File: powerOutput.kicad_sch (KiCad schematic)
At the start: 25 parts, among them J1 Screw_Terminal_01x02, J10 Screw_Terminal_01x04, J11 Screw_Terminal_01x04, J12 Screw_Terminal_01x04, J9 Screw_Terminal_01x04, K1 SANYOU_SRD-S-124D, K2 SANYOU_SRD-S-124D, K3 SANYOU_SRD-S-124D, K4 SANYOU_SRD-S-124D, K5 SANYOU_SRD-S-124D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

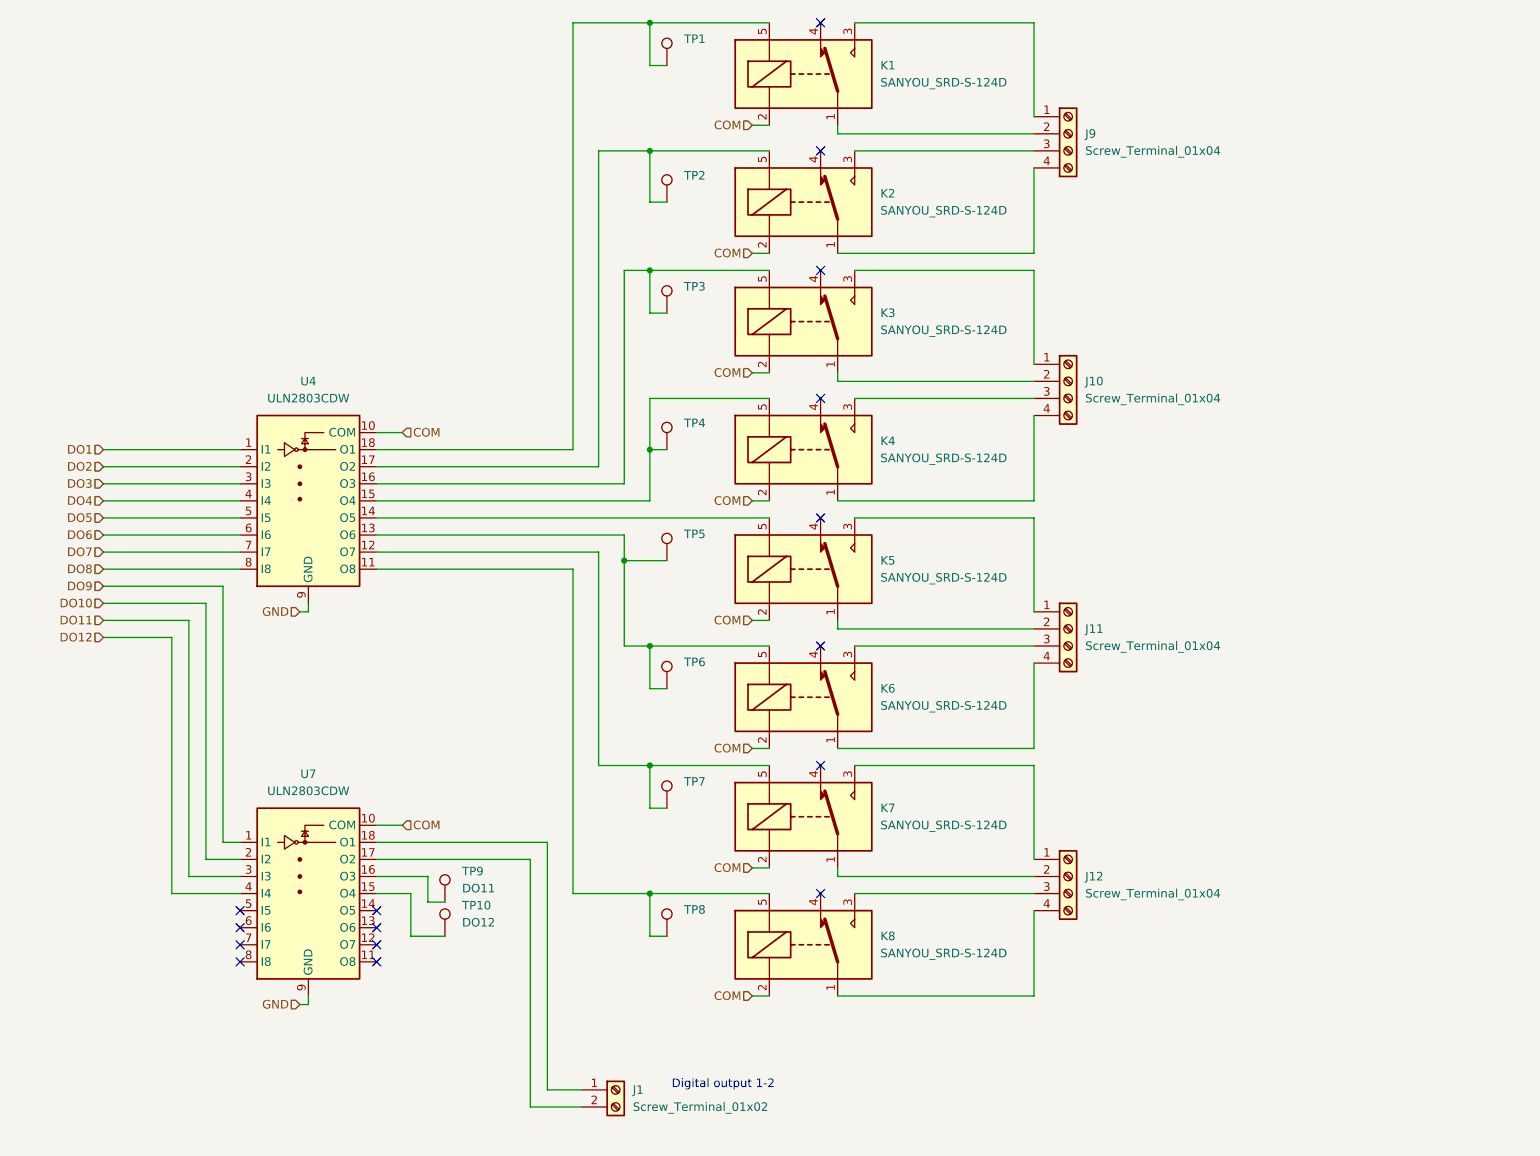
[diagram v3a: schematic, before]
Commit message: added fuse and c for 7805
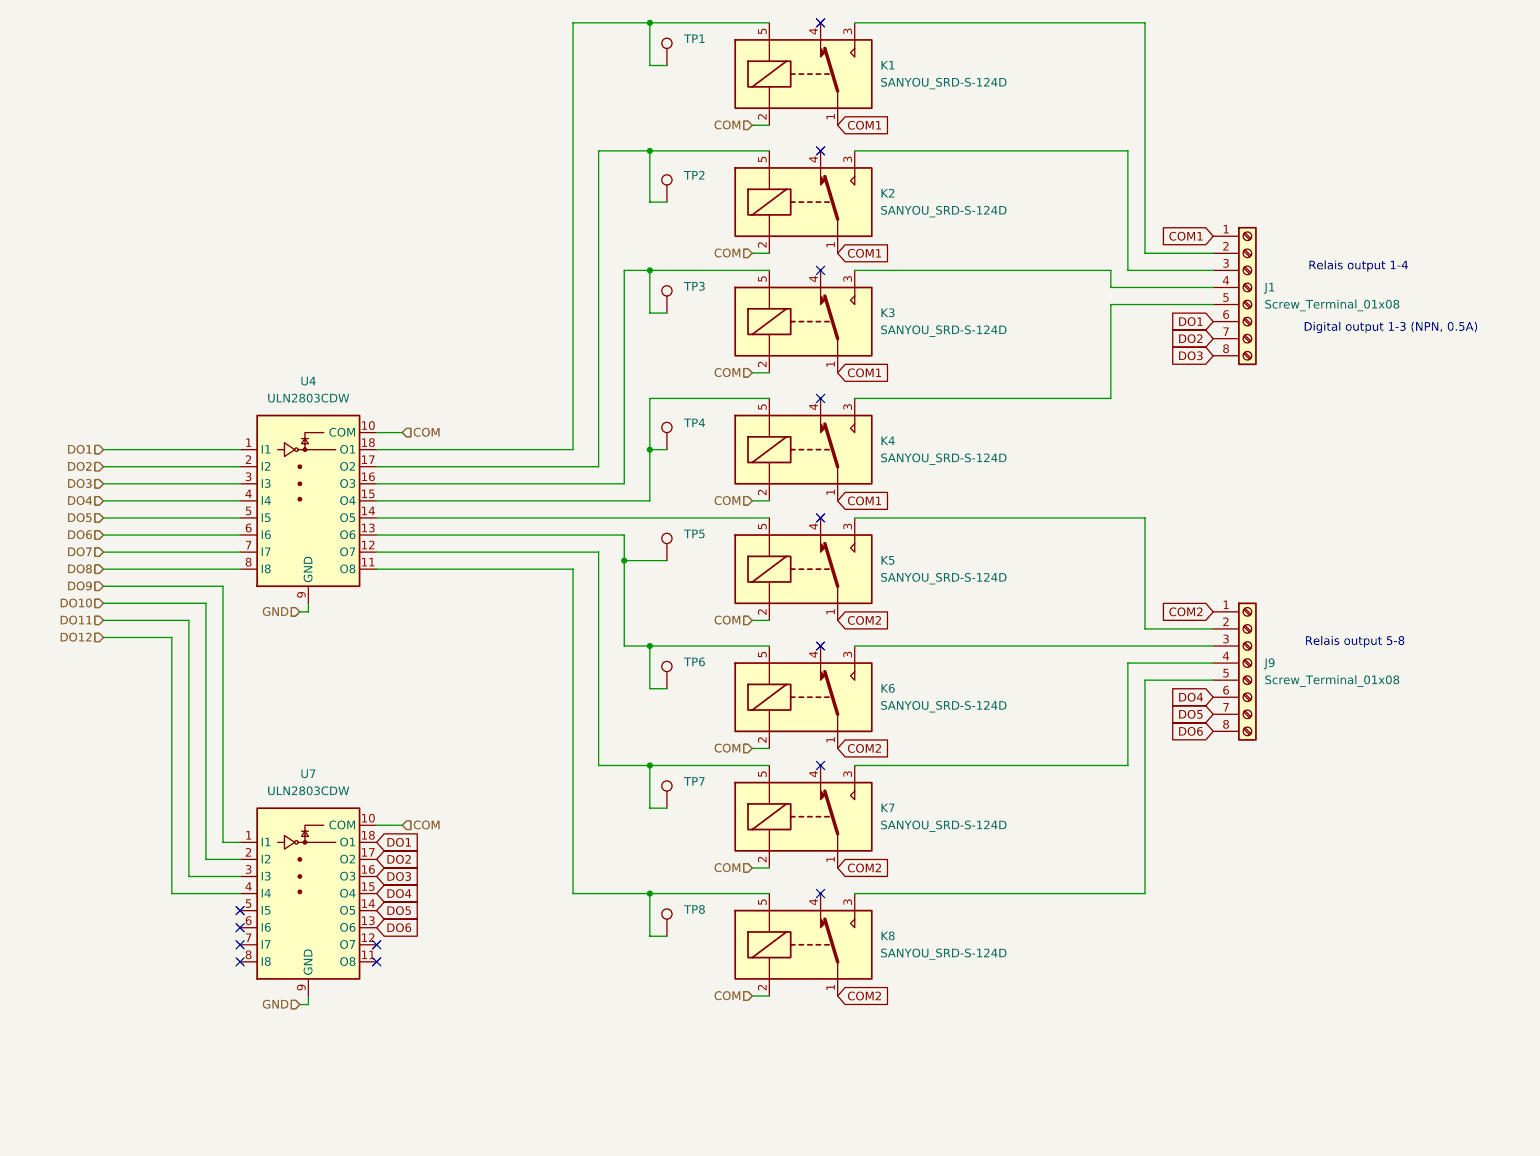
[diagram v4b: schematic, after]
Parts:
- removed J1: Screw_Terminal_01x02, Connector_Phoenix_MC:PhoenixContact_MC_1,5_2-G-3.5_1x02_P3.50mm_Horizontal, symbol Connector:Screw_Terminal_01x02
- removed J10, J11, J12, J9: Screw_Terminal_01x04, Connector_Phoenix_MC:PhoenixContact_MC_1,5_4-G-3.5_1x04_P3.50mm_Horizontal, symbol Connector:Screw_Terminal_01x04
- removed TP10: DO12, TestPoint:TestPoint_Plated_Hole_D2.0mm, symbol Connector:TestPoint
- removed TP9: DO11, TestPoint:TestPoint_Plated_Hole_D2.0mm, symbol Connector:TestPoint
- added J1, J9: Screw_Terminal_01x08, TerminalBlock_RND:TerminalBlock_RND_205-00293_1x08_P5.08mm_Horizontal, symbol Connector:Screw_Terminal_01x08
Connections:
- net DO1: now also U7.18 (O1), J1.6 (Pin_6)
- net DO2: now also U7.17 (O2), J1.7 (Pin_7)
- net DO3: now also U7.16 (O3), J1.8 (Pin_8)
- net DO4: now also U7.15 (O4), J9.6 (Pin_6)
- net DO5: now also U7.14 (O5), J9.7 (Pin_7)
- net DO6: now also U7.13 (O6), J9.8 (Pin_8)
- net at K5.3: now also J9.2 (Pin_2)
- net COM2: now reaches K5.1
- net COM2: now also K6.1, K7.1, K8.1, J9.1 (Pin_1)
- net at K6.3: now also J9.3 (Pin_3)
- net COM1: now reaches K1.1
- net COM1: now also K2.1, K3.1, K4.1, J1.1 (Pin_1)
- net at K1.3: now also J1.2 (Pin_2)
- net at K8.3: now also J9.5 (Pin_5)
- net at K2.3: now also J1.3 (Pin_3)
- net at K4.3: now also J1.5 (Pin_5)
- net at K7.3: now also J9.4 (Pin_4)
- net at K3.3: now also J1.4 (Pin_4)
- no-connect marks 16 -> 14
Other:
- note added: "Digital output 1-3 (NPN, 0.5A)"
- note added: "Relais output 1-4"
- note added: "Relais output 5-8"
- note removed: "Digital output 1-2"

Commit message: hat routing finished
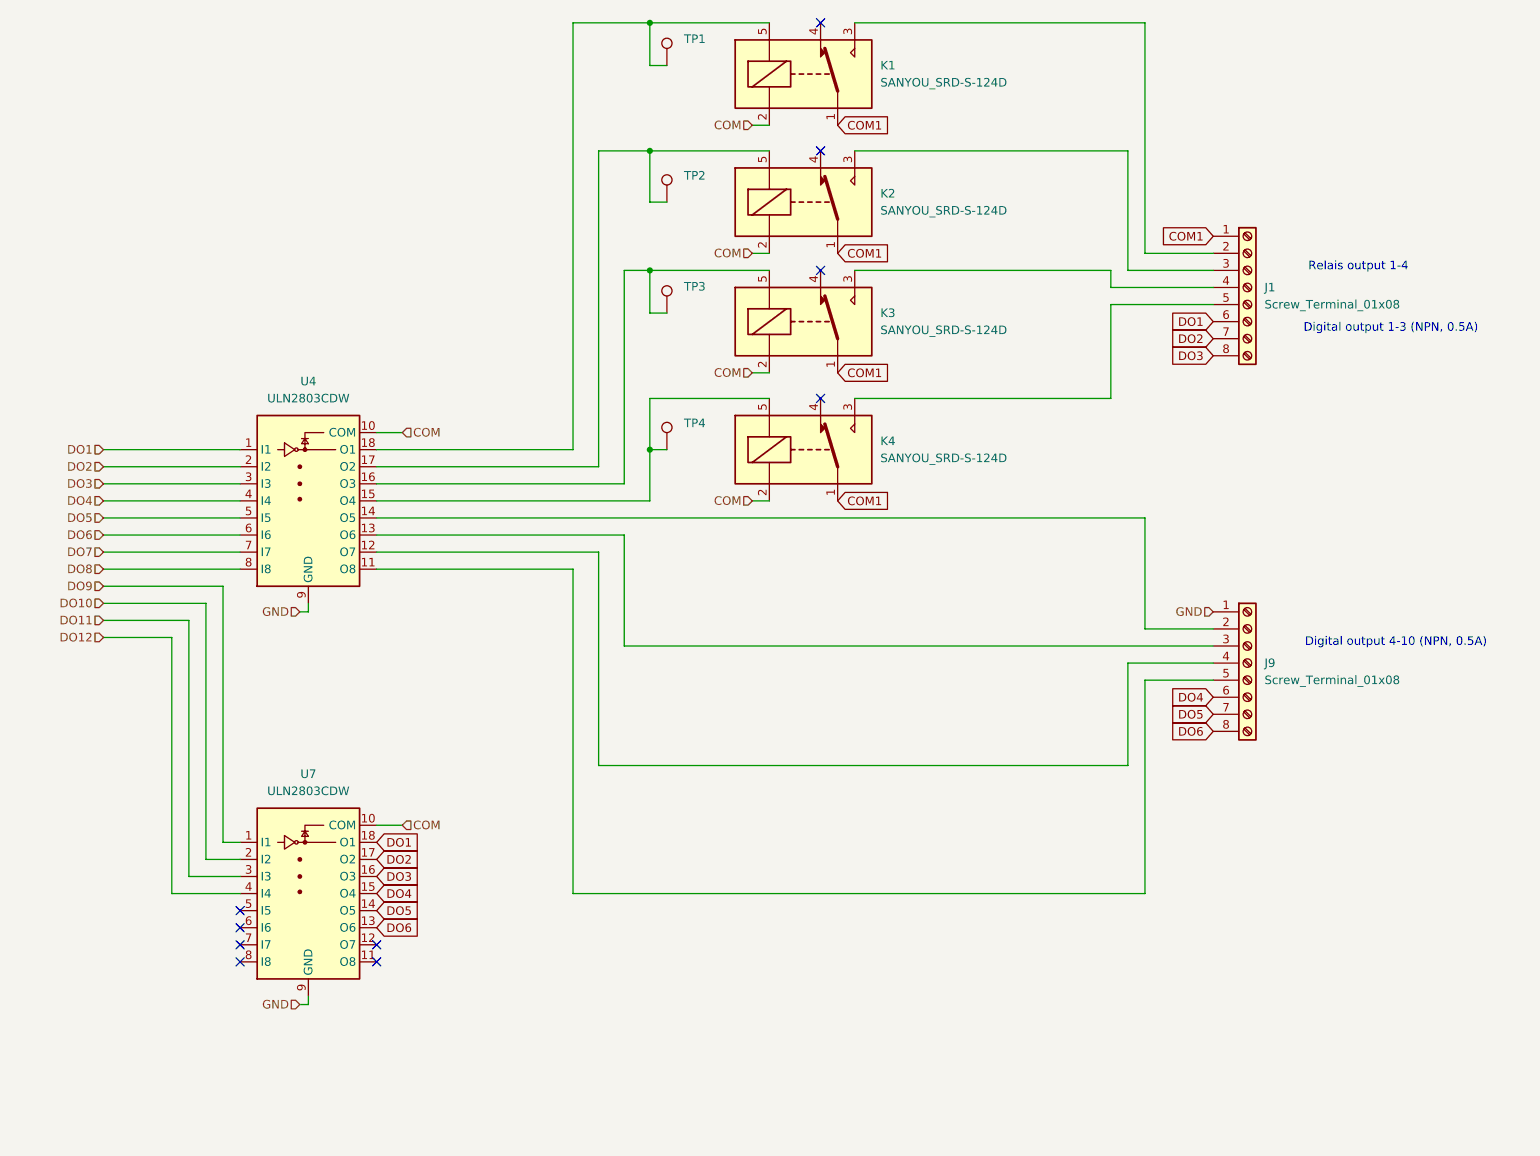
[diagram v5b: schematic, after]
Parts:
- removed K5, K6, K7, K8: SANYOU_SRD-S-124D, Relay_THT:Relay_SPDT_SANYOU_SRD_Series_Form_C, symbol Relay:SANYOU_SRD_Form_C
- removed TP5, TP6, TP7, TP8: ~, TestPoint:TestPoint_Pad_D1.5mm, symbol Connector:TestPoint
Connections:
- net COM2 is gone; now on net GND: J9.1 (Pin_1)
- net at U4.11 (O8): now also J9.5 (Pin_5)
- net at U4.12 (O7): now also J9.4 (Pin_4)
- net at J9.2 (Pin_2): now also U4.14 (O5)
- net at J9.3 (Pin_3): now also U4.13 (O6)
- no-connect marks 14 -> 10
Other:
- note added: "Digital output 4-10 (NPN, 0.5A)"
- note removed: "Relais output 5-8"

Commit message: started base layout
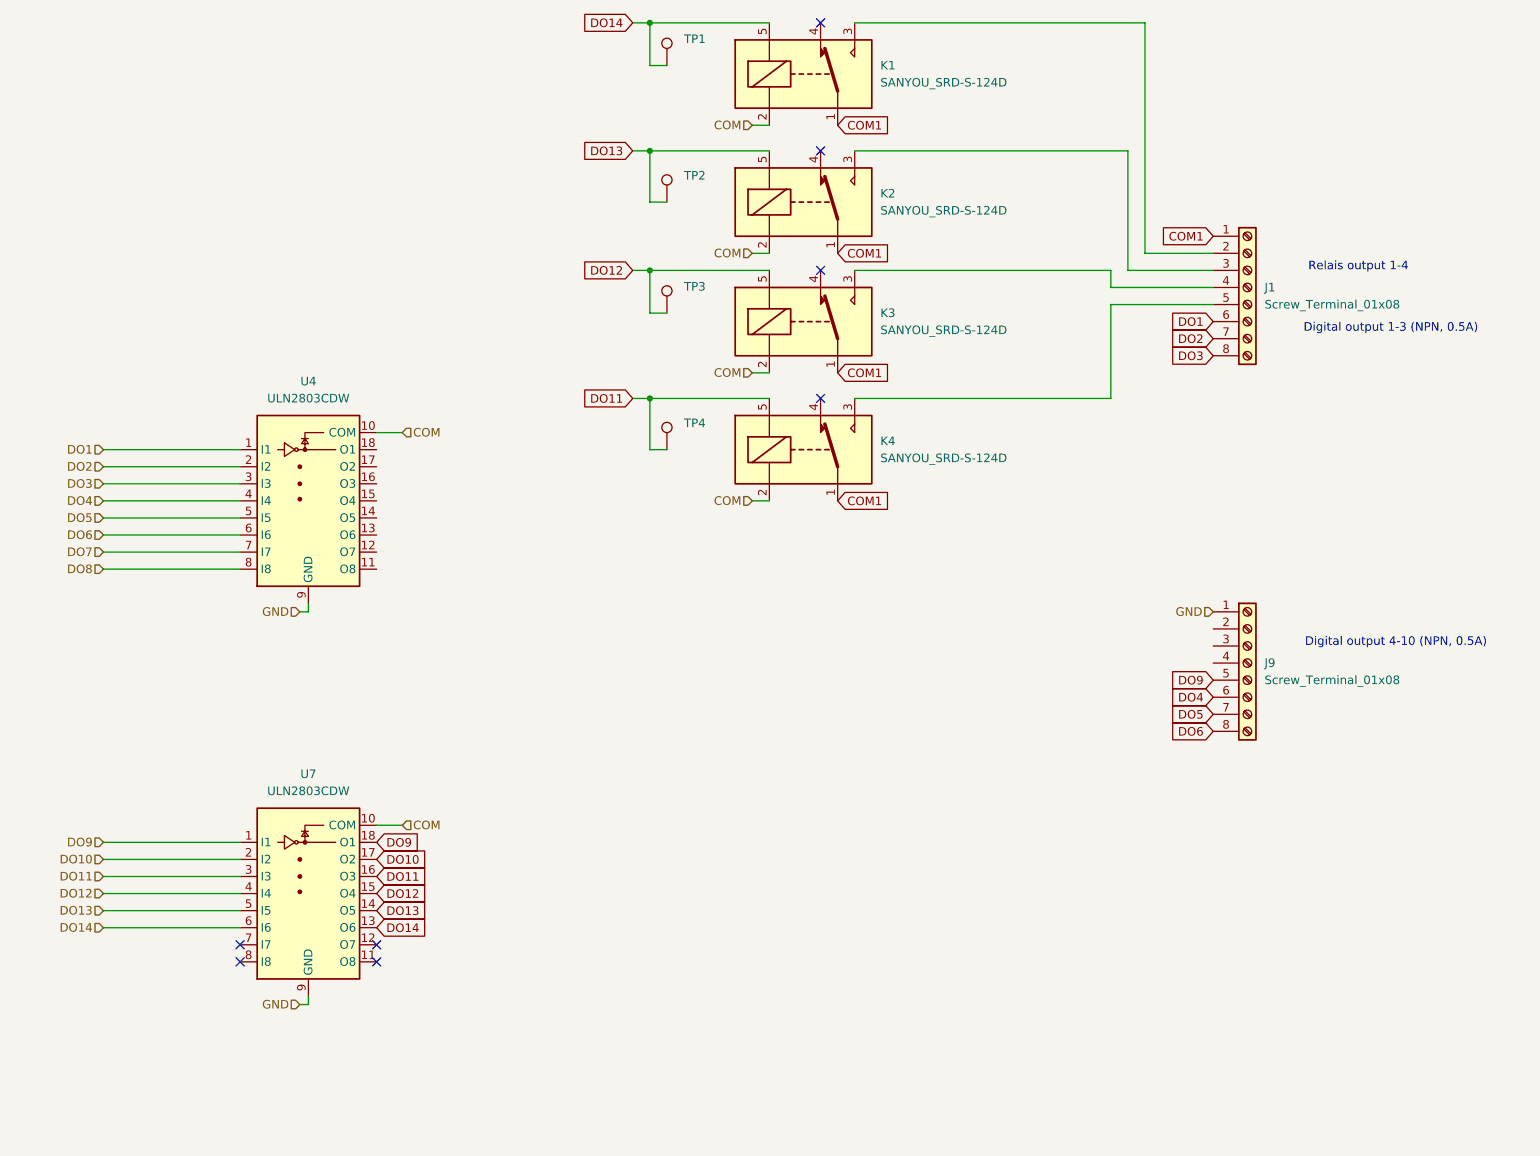
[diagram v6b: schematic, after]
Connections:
- net DO1: no longer U7.18 (O1)
- net DO10: now also U7.17 (O2)
- net DO11: now also K4.5, TP4.1, U7.16 (O3)
- net DO12: now also K3.5, TP3.1, U7.15 (O4)
- net DO2: no longer U7.17 (O2)
- net DO3: no longer U7.16 (O3)
- net DO4: no longer U7.15 (O4)
- net DO5: no longer U7.14 (O5)
- net DO6: no longer U7.13 (O6)
- net DO9: now also J9.5 (Pin_5), U7.18 (O1)
- net DO14: now reaches K1.5, TP1.1
- net DO14: now also U7.13 (O6), U7.6 (I6); no longer U4.18 (O1)
- net at J9.2 (Pin_2): no longer U4.14 (O5)
- net at J9.3 (Pin_3): no longer U4.13 (O6)
- net at J9.4 (Pin_4): no longer U4.12 (O7)
- net at U4.11 (O8): no longer J9.5 (Pin_5)
- net DO13: now reaches K2.5, TP2.1
- net DO13: now also U7.14 (O5), U7.5 (I5); no longer U4.17 (O2)
- now unconnected: U4.15 (O4), U4.16 (O3)
- no-connect marks 10 -> 8

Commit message: von ben
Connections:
- net DO10: no longer U7.17 (O2)
- net DO11: no longer K4.5, TP4.1, U7.16 (O3)
- net DO12: no longer K3.5, TP3.1, U7.15 (O4)
- net DO13: no longer K2.5, TP2.1, U7.14 (O5)
- net DO14: no longer K1.5, TP1.1, U7.13 (O6)
- net DO9: no longer U7.18 (O1)
- new net DO.10: U7.17 (O2)
- new net DO.11: K4.5, TP4.1, U7.16 (O3)
- new net DO.12: K3.5, TP3.1, U7.15 (O4)
- new net DO.13: K2.5, TP2.1, U7.14 (O5)
- new net DO.14: K1.5, TP1.1, U7.13 (O6)
- new net DO.9: U7.18 (O1)
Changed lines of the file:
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@@
 		)
 	)
-	(global_label "DO12"
+	(global_label "DO.12"
 		(shape input)
 		(at 66.04 143.51 0)
@@
 		)
 		(property "Intersheetrefs" "${INTERSHEET_REFS}"
-			(at 74.0447 143.51 0)
-			(effects
-				(font
-					(size 1.27 1.27)
-				)
-				(justify left)
-			)
-		)
-	)
-	(global_label "DO10"
+			(at 74.6495 143.51 0)
+			(effects
+				(font
+					(size 1.27 1.27)
+				)
+				(justify left)
+			)
+		)
+	)
+	(global_label "DO.10"
 		(shape input)
 		(at 66.04 138.43 0)
@@
 		)
 		(property "Intersheetrefs" "${INTERSHEET_REFS}"
-			(at 74.0447 138.43 0)
+			(at 74.6495 138.43 0)
 			(effects
 				(font
@@
 		)
 	)
-	(global_label "DO14"
+	(global_label "DO.14"
 		(shape input)
 		(at 66.04 148.59 0)
@@
 		)
 		(property "Intersheetrefs" "${INTERSHEET_REFS}"
-			(at 74.0447 148.59 0)
+			(at 74.6495 148.59 0)
 			(effects
 				(font
@@
 		)
 	)
-	(global_label "DO12"
+	(global_label "DO.12"
 		(shape input)
 		(at 104.14 50.8 180)
@@
 		)
 		(property "Intersheetrefs" "${INTERSHEET_REFS}"
-			(at 96.1353 50.8 0)
+			(at 95.5305 50.8 0)
 			(effects
 				(font
@@
 		)
 	)
-	(global_label "DO13"
+	(global_label "DO.13"
 		(shape input)
 		(at 66.04 146.05 0)
@@
 		)
 		(property "Intersheetrefs" "${INTERSHEET_REFS}"
-			(at 74.0447 146.05 0)
+			(at 74.6495 146.05 0)
 			(effects
 				(font
@@
 		)
 	)
-	(global_label "DO9"
+	(global_label "DO.9"
 		(shape input)
 		(at 66.04 135.89 0)
@@
 		)
 		(property "Intersheetrefs" "${INTERSHEET_REFS}"
-			(at 72.8352 135.89 0)
+			(at 73.44 135.89 0)
 			(effects
 				(font
@@
 		)
 	)
-	(global_label "DO13"
+	(global_label "DO.13"
 		(shape input)
 		(at 104.14 33.02 180)
@@
 		)
 		(property "Intersheetrefs" "${INTERSHEET_REFS}"
-			(at 96.1353 33.02 0)
-			(effects
-				(font
-					(size 1.27 1.27)
-				)
-				(justify right)
-			)
-		)
-	)
-	(global_label "DO11"
+			(at 95.5305 33.02 0)
+			(effects
+				(font
+					(size 1.27 1.27)
+				)
+				(justify right)
+			)
+		)
+	)
+	(global_label "DO.11"
 		(shape input)
 		(at 66.04 140.97 0)
@@
 		)
 		(property "Intersheetrefs" "${INTERSHEET_REFS}"
-			(at 74.0447 140.97 0)
+			(at 74.6495 140.97 0)
 			(effects
 				(font
@@
 		)
 	)
-	(global_label "DO11"
+	(global_label "DO.11"
 		(shape input)
 		(at 104.14 69.85 180)
@@
 		)
 		(property "Intersheetrefs" "${INTERSHEET_REFS}"
-			(at 96.1353 69.85 0)
+			(at 95.5305 69.85 0)
 			(effects
 				(font
@@
 		)
 	)
-	(global_label "DO14"
+	(global_label "DO.14"
 		(shape input)
 		(at 104.14 13.97 180)
@@
 		)
 		(property "Intersheetrefs" "${INTERSHEET_REFS}"
-			(at 96.1353 13.97 0)
-			(effects
-				(font
+			(at 95.5305 13.97 0)
+			(effects
+				(font
